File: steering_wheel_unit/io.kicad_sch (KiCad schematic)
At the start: 45 parts, among them U3 SN65HVD232

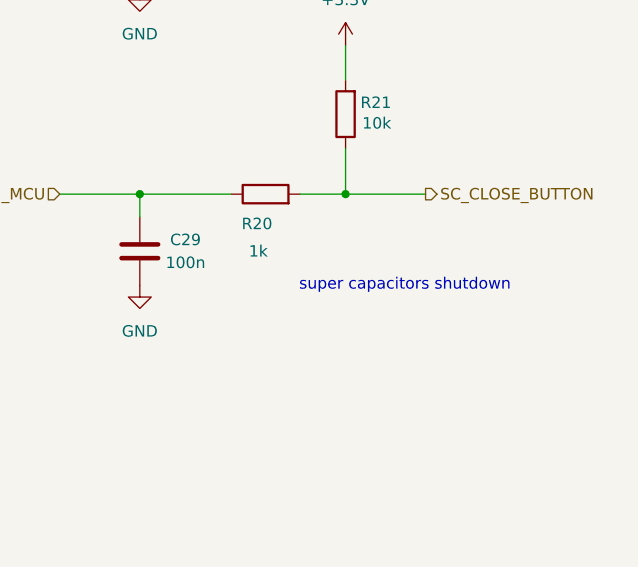
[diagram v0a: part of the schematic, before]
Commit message: Add dimensions
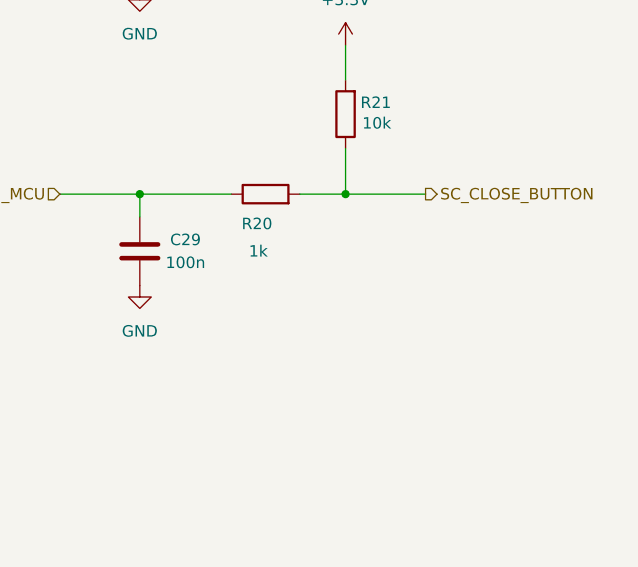
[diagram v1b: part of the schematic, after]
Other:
- note removed: "super capacitors shutdown"
- title: (none) -> Steering_wheel_unit_io
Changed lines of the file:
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@@
 	(generator_version "9.0")
 	(paper "A4")
+	(title_block
+		(title "Steering_wheel_unit_io")
+		(date "2025-03-22")
+	)
 	(text "Functional buttons"
 		(exclude_from_sim no)
@@
 			)
 		)
-	)
-	(text "super capacitors shutdown\n"
-		(exclude_from_sim no)
-		(at 263.144 152.4 0)
-		(effects
-			(font
-				(size 1.27 1.27)
-			)
-		)
